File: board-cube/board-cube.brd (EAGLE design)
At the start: 100 x 100 mm, 125 parts, among them IC1 MSP430FR5739DA, J1 TM4_SHIELD, Q1 BSS84, U1 TPS79933QDDCRQ1, U2 TPS79933QDDCRQ1, X1 SMA-142-0711-821/826, X10 SMA-142-0711-821/826, X2 SMA-142-0711-821/826, X3 SMA-142-0711-821/826, X4 SMA-142-0711-821/826, X5 SMA-142-0711-821/826, X6 SMA-142-0711-821/826, X7 SMA-142-0711-821/826, X8 SMA-142-0711-821/826, X9 SMA-142-0711-821/826

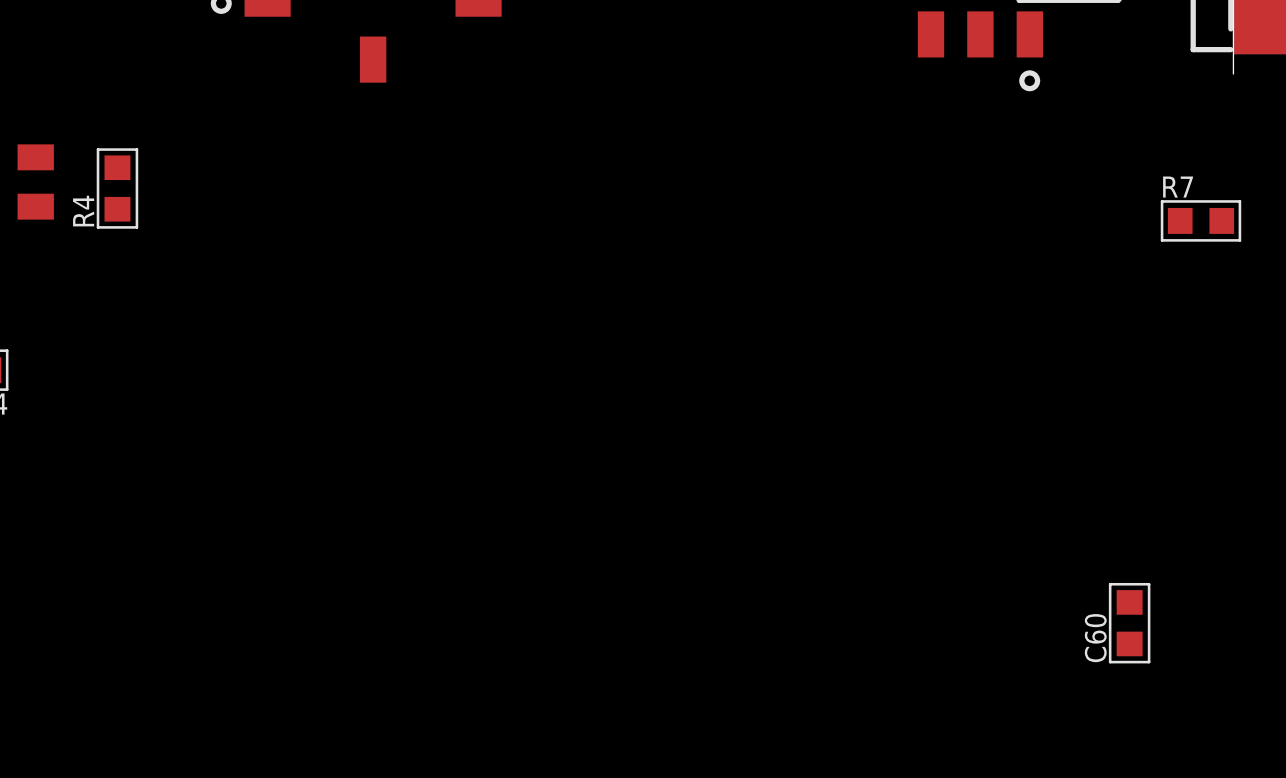
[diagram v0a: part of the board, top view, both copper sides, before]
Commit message: Add 434MHz SAW and 2x SMA Connectors to sch,lbr.
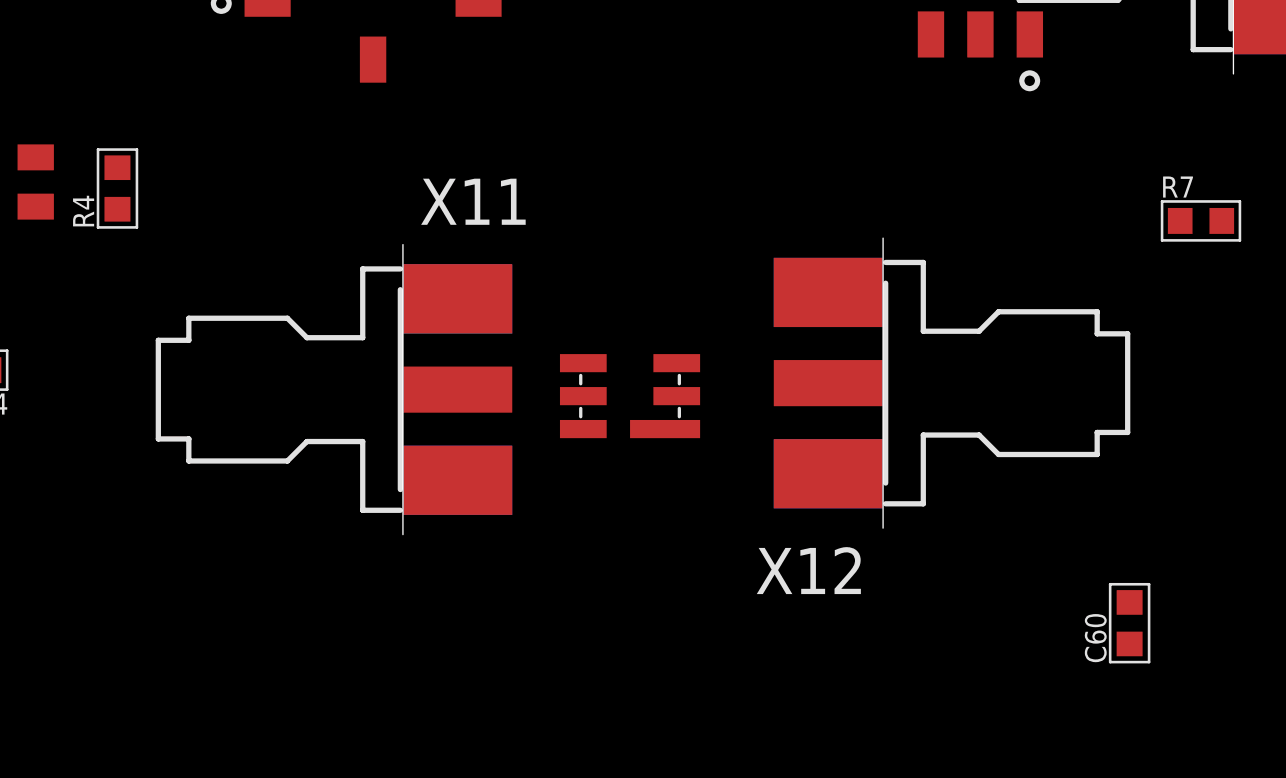
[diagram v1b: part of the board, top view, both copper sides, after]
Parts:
- added U$7: GOLLEDGE_SAW_FILTER, Ava:GOLLEDGE_SAW
- added X11, X12: SMA-142-0711-821/826, con-coax:J502-ND-142-0711-821/826
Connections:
- new net N$43: U$7.E, X11.1
- new net N$44: U$7.B, X12.1
- net GND: now also U$7.A, U$7.C, U$7.D, U$7.F
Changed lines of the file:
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@@
 <element name="LED7" library="dtb" package="CHIP-LED0603" value="" x="19.75" y="56" rot="R90"/>
 <element name="R14" library="passives-7351" package="R0603-N" value="" x="23.75" y="55.75" rot="R180"/>
+<element name="U$7" library="Ava" package="GOLLEDGE_SAW" value="GOLLEDGE_SAW_FILTER" x="49.25" y="54.75"/>
+<element name="X11" library="con-coax" package="J502-ND-142-0711-821/826" value="SMA-142-0711-821/826" x="40.5" y="55">
+<attribute name="OC_NEWARK" value="16F3627" x="40.5" y="55" size="1.778" layer="27" display="off"/>
+<attribute name="MPN" value="142-0711-821" x="40.5" y="55" size="1.778" layer="27" display="off"/>
+<attribute name="MF" value="JOHNSON COMPONENTS" x="40.5" y="55" size="1.778" layer="27" display="off"/>
+<attribute name="OC_FARNELL" value="1019328" x="40.5" y="55" size="1.778" layer="27" display="off"/>
+</element>
+<element name="X12" library="con-coax" package="J502-ND-142-0711-821/826" value="SMA-142-0711-821/826" x="59" y="55.25" rot="R180">
+<attribute name="OC_NEWARK" value="16F3627" x="59" y="55.25" size="1.778" layer="27" rot="R180" display="off"/>
+<attribute name="MPN" value="142-0711-821" x="59" y="55.25" size="1.778" layer="27" rot="R180" display="off"/>
+<attribute name="MF" value="JOHNSON COMPONENTS" x="59" y="55.25" size="1.778" layer="27" rot="R180" display="off"/>
+<attribute name="OC_FARNELL" value="1019328" x="59" y="55.25" size="1.778" layer="27" rot="R180" display="off"/>
+</element>
 </elements>
 <signals>
@@
 <wire x1="56.25" y1="20" x2="54.7428" y2="20" width="0.2" layer="1"/>
 <wire x1="54.7428" y1="20" x2="54.7178" y2="19.975" width="0.2" layer="1"/>
+<wire x1="59.3" y1="20" x2="59.3" y2="20.45" width="0.2" layer="1"/>
+<wire x1="59.3" y1="20.45" x2="59" y2="20.75" width="0.2" layer="1"/>
+<contactref element="U$7" pad="A"/>
+<contactref element="U$7" pad="F"/>
+<contactref element="U$7" pad="C"/>
+<contactref element="U$7" pad="D"/>
 <wire x1="97.8846" y1="70.4946" x2="97.8846" y2="70.4946" width="0" layer="19" extent="1-16"/>
 <wire x1="97.8846" y1="63.5054" x2="97.8846" y2="70.4946" width="0" layer="19" extent="16-16"/>
@@
 <wire x1="-39.7946" y1="89.8546" x2="-39.7946" y2="82.8654" width="0" layer="19" extent="1-1"/>
 <wire x1="-39.7946" y1="89.8546" x2="-39.7946" y2="89.8546" width="0" layer="19" extent="1-16"/>
-<wire x1="59.3" y1="20" x2="59.3" y2="20.45" width="0.2" layer="1"/>
-<wire x1="59.3" y1="20.45" x2="59" y2="20.75" width="0.2" layer="1"/>
+<wire x1="51.05" y1="56.02" x2="6.5" y2="3.25" width="0" layer="19" extent="1-16"/>
+<wire x1="50.6" y1="53.48" x2="51.05" y2="56.02" width="0" layer="19" extent="1-1"/>
+<wire x1="47.45" y1="53.48" x2="50.6" y2="53.48" width="0" layer="19" extent="1-1"/>
+<wire x1="47.45" y1="56.02" x2="47.45" y2="53.48" width="0" layer="19" extent="1-1"/>
 </signal>
 <signal name="N$7">
@@
 <wire x1="22.95" y1="55.75" x2="20.5" y2="56" width="0" layer="19" extent="1-1"/>
 </signal>
+<signal name="N$43">
+<contactref element="X11" pad="1"/>
+<contactref element="U$7" pad="E"/>
+<wire x1="42.6154" y1="55" x2="47.45" y2="54.75" width="0" layer="19" extent="1-1"/>
+</signal>
+<signal name="N$44">
+<contactref element="U$7" pad="B"/>
+<contactref element="X12" pad="1"/>
+<wire x1="51.05" y1="54.75" x2="56.8846" y2="55.25" width="0" layer="19" extent="1-1"/>
+</signal>
 </signals>

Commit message: added alternate PA
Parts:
- removed IC1: MSP430FR5739DA, Mine:TSSOP38
- removed J1: TM4_SHIELD, cube-parts:LAUNCHPAD_SHIELD
- removed JP6: (no value), SparkFun-Connectors:1X04
- added C61: 220p, passives-7351:C0603-N
- added C62: 33p, passives-7351:C0603-N
- added C63, C68: 100p, passives-7351:C0603-N
- added C64: 4.7u, passives-7351:C0603-N
- added C65: 1n, passives-7351:C0603-N
- added C66: 3.3p, passives-7351:C0603-N
- added C67, C69: 1u, passives-7351:C0603-N
- added C70: 15p, passives-7351:C0603-N
- added C71: 27p, passives-7351:C0603-N
- added IC3: MMZ09332BT1, CubeSat3:QFN3X3-6
- added L10, L14, L15, L16: 33n, passives-7351:L0603-N
- added L17: 22n, passives-7351:L0603-N
- added R15: 2.2k, passives-7351:R0603-N
- added R16: 1.8k, passives-7351:R0603-N
- added X13, X14, X15: BU-SMA-V, con-coax:BU-SMA-V
- IC2: value PA -> LHA1+
- X1, X10, X11, X12, X2, X3, X4, X5, X6, X7, X8, X9: value SMA-142-0711-821/826 -> BU-SMA-V; device con-coax:J502-ND-142-0711-821/826 -> con-coax:BU-SMA-V
- moved X9 400.9 mm to (-193.0, -223.0), turned to 0 degrees
- moved X8 400.3 mm to (-176.0, -223.0), turned to 0 degrees
- moved X10 391.8 mm to (-184.5, -223.0)
- moved X12 387.0 mm to (-210.0, -223.0), turned to 0 degrees
- moved X7 383.1 mm to (-167.5, -223.0), turned to 0 degrees
- moved X3 375.1 mm to (-235.5, -223.0)
- moved X5 374.2 mm to (-252.5, -223.0)
- moved X11 368.6 mm to (-201.5, -223.0)
- moved X6 363.5 mm to (-159.0, -223.0), turned to 0 degrees
- moved X2 355.8 mm to (-227.0, -223.0)
- moved X4 353.7 mm to (-244.0, -223.0)
- moved X1 335.8 mm to (-218.5, -223.0)
- flipped R14 to the bottom
- renumbered U$2 to IC2
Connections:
- removed net INT_IN: IC1.6, J1.P$37
- removed net INT_OUT: IC1.7, J1.P$39
- removed net N$16: IC1.21
- removed net RST: IC1.22, J1.P$30
- removed net RST_MAINBRD: IC1.5, J1.P$35
- removed net TX_PA_EN: IC1.37
- removed net VCORE: C59.2, IC1.32
- new net N$58: C61.1, L10.1, L14.2
- new net N$64: C61.2, IC3.7, IC3.8, IC3.9, L15.1
- new net N$65: C62.1, L10.2, X15.1
- new net N$66: C63.1, IC3.6
- new net N$67: C64.1, C65.1, L15.2
- new net N$68: C66.1, IC3.11, L16.1
- new net N$69: C67.1, L16.2
- new net N$70: IC3.12, R16.2
- new net N$71: IC3.1, R15.2
- new net N$72: C68.1, C69.1, IC3.2, R15.1, R16.1
- new net N$73: C70.1, L17.1, X14.1
- new net N$74: C71.1, IC3.3, L17.2
- new net N$75: IC3.10
- new net N$76: C59.2
- net +3V3: no longer IC1.34, IC1.4, J1.P$1
- net +5V: no longer J1.P$2
- net A0_CLK: no longer IC1.14
- net A0_CS: no longer IC1.13
- net A0_SIMO: no longer IC1.23
- net A1_RX: no longer IC1.20, J1.P$7
- net A1_TX: no longer IC1.19, J1.P$5
- net B0_CLK: no longer IC1.25
- net B0_CS: no longer IC1.12
- net B0_SIMO: no longer IC1.30
- net GND: now also C62.2, C63.2, C64.2, C65.2, C66.2, C67.2, C68.2, C69.2, C70.2, C71.2, IC3.EXP, L14.1, X1.2, X1.3, X1.4, X1.5, X10.2, X10.3, X10.4, X10.5, X14.2, X14.3, X14.4, X14.5, X15.2, X15.3, X15.4, X15.5, X2.2, X2.3, X2.4, X2.5, X3.2, X3.3, X3.4, X3.5, X4.2, X4.3, X4.4, X4.5, X5.2, X5.3, X5.4, X5.5, X6.2, X6.3, X6.4, X6.5, X7.2, X7.3, X7.4, X7.5, X8.2, X8.3, X8.4, X8.5, X9.2, X9.3, X9.4, X9.5; no longer IC1.3, IC1.33, IC1.38, J1.P$22, J1.P$4, X1.G@1, X1.G@2, X1.G@3, X1.G@4, X10.G@1, X10.G@2, X10.G@3, X10.G@4, X2.G@1, X2.G@2, X2.G@3, X2.G@4, X3.G@1, X3.G@2, X3.G@3, X3.G@4, X4.G@1, X4.G@2, X4.G@3, X4.G@4, X5.G@1, X5.G@2, X5.G@3, X5.G@4, X6.G@1, X6.G@2, X6.G@3, X6.G@4, X7.G@1, X7.G@2, X7.G@3, X7.G@4, X8.G@1, X8.G@2, X8.G@3, X8.G@4, X9.G@1, X9.G@2, X9.G@3, X9.G@4
- net N$15: no longer IC1.18
- net N$17: no longer IC1.17
- net N$27: now also X4.1; no longer X3.1
- net N$28: now also X3.1; no longer X4.1
- net N$37: no longer IC1.16
- net N$38: no longer IC1.15
- net RX_CLK: no longer J1.P$19
- net RX_CS: no longer J1.P$36
- net RX_GPIO0: no longer IC1.27, J1.P$27
- net RX_GPIO2: no longer IC1.28, J1.P$29
- net RX_GPIO3: no longer IC1.29, J1.P$31
- net RX_MISO: no longer IC1.31, J1.P$17
- net RX_MOSI: no longer J1.P$15
- net RX_RST: no longer IC1.9, J1.P$40
- net TX_CLK: no longer J1.P$13
- net TX_CS: no longer J1.P$26
- net TX_GPIO0: no longer IC1.10, J1.P$21
- net TX_GPIO2: no longer IC1.11, J1.P$23
- net TX_GPIO3: no longer IC1.26, J1.P$25
- net TX_MISO: no longer IC1.24, J1.P$34
- net TX_MOSI: no longer J1.P$32
- net TX_RST: no longer IC1.8, J1.P$38
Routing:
- net RX_GPIO3: track 56.7 -> 0.00 mm, vias 2 -> 0
- net RX_GPIO0: track 62.8 -> 8.13 mm, vias 2 -> 0
- net RX_GPIO2: track 54.6 -> 0.00 mm, vias 2 -> 0
- net TX_GPIO0: track 55.0 -> 23.8 mm, vias 2 -> 0
- net TX_CLK: track 88.8 -> 58.3 mm
- net TX_MISO: track 52.0 -> 22.2 mm, vias 4 -> 2
- net TX_GPIO3: track 60.0 -> 30.3 mm, vias 3 -> 1
- net A1_RX: track 35.8 -> 6.76 mm
- net GND: track 40.6 -> 11.6 mm
- net RX_RST: track 27.3 -> 0.00 mm
- net N$15: track 26.3 -> 0.00 mm
- net TX_GPIO2: track 26.2 -> 0.00 mm
- net INT_IN: track 23.9 -> 0.00 mm
- net RX_MISO: track 60.0 -> 36.5 mm
- net N$17: track 23.2 -> 0.00 mm
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
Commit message: adding supervising processor
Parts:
- added C72: (no value), passives-7351:C0805-N
- added C73, C74: 1u, passives-7351:C0603-N
- added C75: 100n, passives-7351:C0603-N
- added IC1: MSP430FR2110PW, CubeSat3:SSOP16
- added JP6, JP7: M02PTH, SparkFun-Connectors:1X02
- added L18, L19, L20: 0R, passives-7351:L0603-N
- added LED8, LED9: (no value), dtb:CHIP-LED0603
- added R17, R19: (no value), passives-7351:R0603-N
- added R18: 4k7, passives-7351:R0603-N
- added X16, X17: BU-SMA-V, con-coax:BU-SMA-V
- C4, C56: value 100n -> dnp
- C57, C58: value 1u -> dnp
- C59: value 470n -> (none); device passives-7351:C0603-N -> passives-7351:C0805-N
- moved R14 519.1 mm to (-294.2, -354.5), flipped to the top, turned to 0 degrees
- moved LED7 514.1 mm to (-294.0, -351.2), turned to 0 degrees
- moved C59 505.6 mm to (-294.2, -342.2), turned to 0 degrees
- moved C56 475.7 mm to (-294.2, -297.2), turned to 0 degrees
- moved C4 474.8 mm to (-294.2, -294.2), turned to 0 degrees
- moved C58 471.0 mm to (-294.2, -303.2), turned to 0 degrees
- moved C57 467.9 mm to (-294.2, -300.2), turned to 0 degrees
- moved X5 428.2 mm to (53.5, 76.6)
- moved X9 413.9 mm to (92.6, 76.6)
- moved X3 400.7 mm to (29.7, 77.4)
- moved X10 394.6 mm to (72.3, 76.6)
- moved X8 394.4 mm to (96.4, 62.2)
- moved X12 385.9 mm to (57.6, 55.0)
- moved X11 368.6 mm to (40.8, 54.8)
- moved U$6 19.6 mm to (82.0, 76.3), turned to 90 degrees
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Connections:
- new net N$16: C4.2, L18.1, X16.1
- new net N$77: C57.2, L19.2, L20.1
- new net N$78: C58.2, L20.2, X17.1
- new net N$79: C25.2, C54.1, C55.1, JP2.1, L5.2, LED8.A
- new net N$80: C73.1, C74.1, C75.1, IC1.5
- net +3V3: no longer C4.1, C56.1, C57.1, C58.1
- net GND: now also C4.1, C56.1, C57.1, C58.1, C59.2, C72.2, C73.2, C74.2, C75.2, IC1.6, R14.2, R17.2, R18.1, R19.2, X16.2, X16.3, X16.4, X16.5, X17.2, X17.3, X17.4, X17.5; no longer C4.2, C56.2, C57.2, C58.2, C59.1
- net N$24: now also C59.1, C64.1, C65.1, C67.1, C68.1, C69.1, C72.1, IC3.2, JP6.1, L15.2, L16.2, R15.1, R16.1; no longer C25.2, C54.1, C55.1, JP2.1, L5.2
- net N$42: now also LED7.C, R14.1; no longer LED7.A, R14.2
- net N$52: now also LED7.A
- net N$6: now also JP6.2
- net N$62: now also JP7.1
- net N$67: now also LED8.C, R17.1; no longer C64.1, C65.1, L15.2
- net N$69: now also JP7.2, R18.2; no longer C67.1, L16.2
- net N$72: now also LED9.C, R19.1; no longer C68.1, C69.1, IC3.2, R15.1, R16.1
- net N$76: now also C56.2, L18.2, L19.1; no longer C59.2

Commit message: rough placement of PA
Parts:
- moved L17 449.7 mm to (56.1, 19.1), turned to 180 degrees
- moved C70 449.1 mm to (58.4, 21.6), turned to 90 degrees
- moved C71 448.7 mm to (55.2, 21.6), turned to 90 degrees
- moved C68 440.0 mm to (56.0, 16.4)
- moved C69 436.5 mm to (52.0, 12.8), turned to 90 degrees
- moved R16 433.8 mm to (53.6, 12.8), turned to 90 degrees
- moved R15 433.1 mm to (55.2, 12.8), turned to 90 degrees
- moved C66 426.2 mm to (49.2, 15.2), turned to 180 degrees
- moved C67 426.0 mm to (48.4, 12.8), turned to 90 degrees
- moved C63 423.4 mm to (50.5, 24.2), turned to 90 degrees
- moved L16 423.4 mm to (50.0, 12.8), turned to 270 degrees
- moved C65 417.3 mm to (45.2, 12.0), turned to 180 degrees
- moved L15 415.6 mm to (46.0, 14.4), turned to 270 degrees
- moved L14 415.2 mm to (44.8, 21.2), turned to 270 degrees
- moved C64 414.4 mm to (45.2, 10.4), turned to 180 degrees
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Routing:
- net N$64: track 0.00 -> 9.04 mm
- net N$71: track 0.00 -> 5.82 mm
- net N$70: track 0.00 -> 5.07 mm
- net N$68: track 0.00 -> 3.91 mm
- net N$24: track 0.00 -> 3.20 mm
- net N$74: track 0.00 -> 3.04 mm
